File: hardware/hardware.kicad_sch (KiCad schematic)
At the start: 1 part, among them U1 CH32V003F4P6

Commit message: add ch32v003 on pcb
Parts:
- added C1, C10, C11, C12, C13, C14, C15, C16, C17, C18, C19, C2, C20, C21, C22, C23, C24, C25, C26, C27, C28, C29, C30, C31, C32, C33, C34, C35, C36, C37, C38, C39, C40, C41, C42, C43, C44, C45, C46, C47, C48, C49, C50, C51, C52, C53, C54, C7, C8, C9: C_Small, Capacitor_SMD:C_0603_1608Metric, symbol Device:C_Small
- added C3, C4, C5, C6: C, Capacitor_SMD:C_0603_1608Metric, symbol Device:C
- added D1, D10, D11, D12, D13, D14, D15, D16, D17, D18, D19, D2, D20, D21, D22, D23, D24, D3, D4, D5, D6, D7, D8, D9: LED, LED_SMD:LED_0603_1608Metric, symbol Device:LED
- added J1: USB_B_Micro, Connector_USB:USB_Micro-B_Amphenol_10118194_Horizontal, symbol Connector:USB_B_Micro
- added R1, R10, R11, R12, R13, R14, R15, R16, R17, R18, R19, R2, R20, R21, R22, R23, R24, R25, R26, R3, R4, R5, R6, R7, R8, R9: R_Small, Resistor_SMD:R_0603_1608Metric, symbol Device:R_Small
- added U10, U11, U12, U13, U14, U15, U16, U17, U18, U19, U2, U20, U21, U22, U23, U24, U25, U26, U27, U5, U6, U7, U8, U9: CH32V003F4P6, CH32V003F4P6:SOP65P640X121-20N, symbol ch32v003:CH32V003F4P6
- added U3: AMS1117-3.3, Package_TO_SOT_SMD:SOT-223-3_TabPin2, symbol Regulator_Linear:AMS1117-3.3
- added U4: CH340C, Package_SO:SOIC-16_3.9x9.9mm_P1.27mm, symbol Interface_USB:CH340C
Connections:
- net SDA: now reaches U1.11 (PC1/SDA/NSS)
- net SDA: now also R2.2, U10.11 (PC1/SDA/NSS), U11.11 (PC1/SDA/NSS), U12.11 (PC1/SDA/NSS), U13.11 (PC1/SDA/NSS), U14.11 (PC1/SDA/NSS), U15.11 (PC1/SDA/NSS), U16.11 (PC1/SDA/NSS), U17.11 (PC1/SDA/NSS), U18.11 (PC1/SDA/NSS), U19.11 (PC1/SDA/NSS), U2.11 (PC1/SDA/NSS), U20.11 (PC1/SDA/NSS), U21.11 (PC1/SDA/NSS), U22.11 (PC1/SDA/NSS), U23.11 (PC1/SDA/NSS), U24.11 (PC1/SDA/NSS), U25.11 (PC1/SDA/NSS), U26.11 (PC1/SDA/NSS), U27.11 (PC1/SDA/NSS), U5.11 (PC1/SDA/NSS), U6.11 (PC1/SDA/NSS), U7.11 (PC1/SDA/NSS), U8.11 (PC1/SDA/NSS), U9.11 (PC1/SDA/NSS)
- net SCL: now reaches U1.12 (PC2/SCL/URTS/T1BKIN)
- net SCL: now also R1.2, U10.12 (PC2/SCL/URTS/T1BKIN), U11.12 (PC2/SCL/URTS/T1BKIN), U12.12 (PC2/SCL/URTS/T1BKIN), U13.12 (PC2/SCL/URTS/T1BKIN), U14.12 (PC2/SCL/URTS/T1BKIN), U15.12 (PC2/SCL/URTS/T1BKIN), U16.12 (PC2/SCL/URTS/T1BKIN), U17.12 (PC2/SCL/URTS/T1BKIN), U18.12 (PC2/SCL/URTS/T1BKIN), U19.12 (PC2/SCL/URTS/T1BKIN), U2.12 (PC2/SCL/URTS/T1BKIN), U20.12 (PC2/SCL/URTS/T1BKIN), U21.12 (PC2/SCL/URTS/T1BKIN), U22.12 (PC2/SCL/URTS/T1BKIN), U23.12 (PC2/SCL/URTS/T1BKIN), U24.12 (PC2/SCL/URTS/T1BKIN), U25.12 (PC2/SCL/URTS/T1BKIN), U26.12 (PC2/SCL/URTS/T1BKIN), U27.12 (PC2/SCL/URTS/T1BKIN), U5.12 (PC2/SCL/URTS/T1BKIN), U6.12 (PC2/SCL/URTS/T1BKIN), U7.12 (PC2/SCL/URTS/T1BKIN), U8.12 (PC2/SCL/URTS/T1BKIN), U9.12 (PC2/SCL/URTS/T1BKIN)
- net DIO0: now reaches U1.18 (PD1/SWIO/T1CH3N/AETR2)
- net RX-PROG: now reaches U1.2 (PD5/UTX/A5)
- net RX-PROG: now also U4.3 (RXD)
- net TX-PROG: now reaches U1.3 (PD6/URX/A6)
- net TX-PROG: now also U4.2 (TXD)
- net GND: now reaches U1.7 (VSS)
- net GND: now also C1.2, C10.2, C11.2, C12.2, C13.2, C14.2, C15.2, C16.2, C17.2, C18.2, C19.2, C2.2, C20.2, C21.2, C22.2, C23.2, C24.2, C25.2, C26.2, C27.2, C28.2, C29.2, C3.2, C30.2, C31.2, C32.2, C33.2, C34.2, C35.2, C36.2, C37.2, C38.2, C39.2, C4.2, C40.2, C41.2, C42.2, C43.2, C44.2, C45.2, C46.2, C47.2, C48.2, C49.2, C5.2, C50.2, C51.2, C52.2, C53.2, C54.2, C6.2, C7.2, C8.2, C9.2, J1.5 (GND), U10.7 (VSS), U11.7 (VSS), U12.7 (VSS), U13.7 (VSS), U14.7 (VSS), U15.7 (VSS), U16.7 (VSS), U17.7 (VSS), U18.7 (VSS), U19.7 (VSS), U2.7 (VSS), U20.7 (VSS), U21.7 (VSS), U22.7 (VSS), U23.7 (VSS), U24.7 (VSS), U25.7 (VSS), U26.7 (VSS), U27.7 (VSS), U3.1 (GND), U4.1 (GND), U5.7 (VSS), U6.7 (VSS), U7.7 (VSS), U8.7 (VSS), U9.7 (VSS)
- net +3V3: now reaches U1.9 (VDD)
- net +3V3: now also C1.1, C10.1, C11.1, C12.1, C13.1, C14.1, C15.1, C16.1, C17.1, C18.1, C19.1, C2.1, C20.1, C21.1, C22.1, C23.1, C24.1, C25.1, C26.1, C27.1, C28.1, C29.1, C30.1, C31.1, C32.1, C33.1, C34.1, C35.1, C36.1, C37.1, C38.1, C39.1, C4.1, C40.1, C41.1, C42.1, C43.1, C44.1, C45.1, C46.1, C47.1, C48.1, C49.1, C5.1, C50.1, C51.1, C52.1, C53.1, C54.1, C6.1, C7.1, C8.1, C9.1, R1.1, R10.2, R11.2, R12.2, R13.2, R14.2, R15.2, R16.2, R17.2, R18.2, R19.2, R2.1, R20.2, R21.2, R22.2, R23.2, R24.2, R25.2, R26.2, R3.2, R4.2, R5.2, R6.2, R7.2, R8.2, R9.2, U10.9 (VDD), U11.9 (VDD), U12.9 (VDD), U13.9 (VDD), U14.9 (VDD), U15.9 (VDD), U16.9 (VDD), U17.9 (VDD), U18.9 (VDD), U19.9 (VDD), U2.9 (VDD), U20.9 (VDD), U21.9 (VDD), U22.9 (VDD), U23.9 (VDD), U24.9 (VDD), U25.9 (VDD), U26.9 (VDD), U27.9 (VDD), U3.2 (VO), U4.16 (VCC), U4.4 (V3), U5.9 (VDD), U6.9 (VDD), U7.9 (VDD), U8.9 (VDD), U9.9 (VDD)
- new net: D16.2 (A), R18.1
- new net: D7.2 (A), R9.1
- new net: D8.2 (A), R10.1
- new net: D16.1 (K), U19.20 (PD3/A4/T2CH2/AETR/UCTS)
- new net: D23.1 (K), U26.20 (PD3/A4/T2CH2/AETR/UCTS)
- new net: D7.1 (K), U10.20 (PD3/A4/T2CH2/AETR/UCTS)
- new net: D14.1 (K), U17.20 (PD3/A4/T2CH2/AETR/UCTS)
- new net: D14.2 (A), R16.1
- new net: D9.1 (K), U12.20 (PD3/A4/T2CH2/AETR/UCTS)
- new net: D24.1 (K), U27.20 (PD3/A4/T2CH2/AETR/UCTS)
- new net: D15.2 (A), R17.1
- new net: D22.1 (K), U25.20 (PD3/A4/T2CH2/AETR/UCTS)
- new net: D22.2 (A), R24.1
- new net: D15.1 (K), U18.20 (PD3/A4/T2CH2/AETR/UCTS)
- new net: D12.2 (A), R14.1
- new net: D19.2 (A), R21.1
- new net: D12.1 (K), U15.20 (PD3/A4/T2CH2/AETR/UCTS)
- new net: D6.2 (A), R8.1
- new net: D6.1 (K), U9.20 (PD3/A4/T2CH2/AETR/UCTS)
- new net: D24.2 (A), R26.1
- new net: D13.1 (K), U16.20 (PD3/A4/T2CH2/AETR/UCTS)
- new net: D13.2 (A), R15.1
- new net: D18.1 (K), U21.20 (PD3/A4/T2CH2/AETR/UCTS)
- new net: D8.1 (K), U11.20 (PD3/A4/T2CH2/AETR/UCTS)
- new net: D9.2 (A), R11.1
- new net: D10.1 (K), U13.20 (PD3/A4/T2CH2/AETR/UCTS)
- new net: D2.1 (K), U5.20 (PD3/A4/T2CH2/AETR/UCTS)
- new net: D2.2 (A), R4.1
- new net: D20.1 (K), U23.20 (PD3/A4/T2CH2/AETR/UCTS)
- new net: D11.1 (K), U14.20 (PD3/A4/T2CH2/AETR/UCTS)
- new net: D11.2 (A), R13.1
- new net: D1.1 (K), U2.20 (PD3/A4/T2CH2/AETR/UCTS)
- new net: D4.1 (K), U7.20 (PD3/A4/T2CH2/AETR/UCTS)
- new net: D4.2 (A), R6.1
- new net: D3.1 (K), U6.20 (PD3/A4/T2CH2/AETR/UCTS)
- new net: D20.2 (A), R22.1
- new net: D5.1 (K), U8.20 (PD3/A4/T2CH2/AETR/UCTS)
- new net: D5.2 (A), R7.1
- new net: D10.2 (A), R12.1
- new net: D23.2 (A), R25.1
- new net: D17.1 (K), U20.20 (PD3/A4/T2CH2/AETR/UCTS)
- new net: D17.2 (A), R19.1
- new net: D21.2 (A), R23.1
- new net: D18.2 (A), R20.1
- new net: D19.1 (K), U22.20 (PD3/A4/T2CH2/AETR/UCTS)
- new net: D1.2 (A), R3.1
- new net: D3.2 (A), R5.1
- new net: D21.1 (K), U24.20 (PD3/A4/T2CH2/AETR/UCTS)
- new net +5V: C3.1, J1.1 (VBUS), U3.3 (VI)
- new net D+: J1.3 (D+), U4.5 (UD+)
- new net D-: J1.2 (D-), U4.6 (UD-)
- new net DIO1: U10.18 (PD1/SWIO/T1CH3N/AETR2), U11.18 (PD1/SWIO/T1CH3N/AETR2), U12.18 (PD1/SWIO/T1CH3N/AETR2), U13.18 (PD1/SWIO/T1CH3N/AETR2), U14.18 (PD1/SWIO/T1CH3N/AETR2), U15.18 (PD1/SWIO/T1CH3N/AETR2), U16.18 (PD1/SWIO/T1CH3N/AETR2), U17.18 (PD1/SWIO/T1CH3N/AETR2), U18.18 (PD1/SWIO/T1CH3N/AETR2), U19.18 (PD1/SWIO/T1CH3N/AETR2), U2.18 (PD1/SWIO/T1CH3N/AETR2), U20.18 (PD1/SWIO/T1CH3N/AETR2), U21.18 (PD1/SWIO/T1CH3N/AETR2), U22.18 (PD1/SWIO/T1CH3N/AETR2), U23.18 (PD1/SWIO/T1CH3N/AETR2), U24.18 (PD1/SWIO/T1CH3N/AETR2), U25.18 (PD1/SWIO/T1CH3N/AETR2), U26.18 (PD1/SWIO/T1CH3N/AETR2), U27.18 (PD1/SWIO/T1CH3N/AETR2), U5.18 (PD1/SWIO/T1CH3N/AETR2), U6.18 (PD1/SWIO/T1CH3N/AETR2), U7.18 (PD1/SWIO/T1CH3N/AETR2), U8.18 (PD1/SWIO/T1CH3N/AETR2), U9.18 (PD1/SWIO/T1CH3N/AETR2)
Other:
- note added: "CONNECTOR"
- note added: "PROGRAM"
- note added: "REGULATOR"
- moved on the sheet: U1

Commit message: add wiring ch32v006
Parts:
- added D25: LED, LED_SMD:LED_0603_1608Metric, symbol Device:LED
- added J2: RJ45_Hanrun_HR911105A_Horizontal, Connector_RJ:RJ45_Hanrun_HR911105A_Horizontal, symbol Connector:RJ45_Hanrun_HR911105A_Horizontal
- added J3: Conn_02x05_Odd_Even, symbol Connector_Generic:Conn_02x05_Odd_Even
- added R27, R28, R29: R_Small, Resistor_SMD:R_0603_1608Metric, symbol Device:R_Small
- added TP1, TP10, TP11, TP12, TP13, TP14, TP15, TP16, TP17, TP18, TP19, TP2, TP20, TP21, TP22, TP23, TP24, TP25, TP3, TP4, TP5, TP6, TP7, TP8, TP9: TestPoint, TestPoint:TestPoint_Pad_1.0x1.0mm, symbol Connector:TestPoint
- added U28: CH32V307RCT6, symbol WCH:CH32V307RCT6
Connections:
- net +3V3: now also J2.4 (TCT), J2.5 (RCT), J3.7 (Pin_7), R27.2, R28.1, R29.1
- net GND: now also J2.8, J2.SH, J3.5 (Pin_5), U28.12 (VSSA), U28.18 (VSS_4), U28.31 (VSS_1), U28.47 (VSS_2), U28.63 (VSS_3)
- net at U1.20 (PD3/A4/T2CH2/AETR/UCTS): now also D25.1 (K)
- net DIO0: no longer names the net of U1.18 (PD1/SWIO/T1CH3N/AETR2)
- net DIO0: now also TP25.1
- removed net DIO1: U10.18 (PD1/SWIO/T1CH3N/AETR2), U11.18 (PD1/SWIO/T1CH3N/AETR2), U12.18 (PD1/SWIO/T1CH3N/AETR2), U13.18 (PD1/SWIO/T1CH3N/AETR2), U14.18 (PD1/SWIO/T1CH3N/AETR2), U15.18 (PD1/SWIO/T1CH3N/AETR2), U16.18 (PD1/SWIO/T1CH3N/AETR2), U17.18 (PD1/SWIO/T1CH3N/AETR2), U18.18 (PD1/SWIO/T1CH3N/AETR2), U19.18 (PD1/SWIO/T1CH3N/AETR2), U2.18 (PD1/SWIO/T1CH3N/AETR2), U20.18 (PD1/SWIO/T1CH3N/AETR2), U21.18 (PD1/SWIO/T1CH3N/AETR2), U22.18 (PD1/SWIO/T1CH3N/AETR2), U23.18 (PD1/SWIO/T1CH3N/AETR2), U24.18 (PD1/SWIO/T1CH3N/AETR2), U25.18 (PD1/SWIO/T1CH3N/AETR2), U26.18 (PD1/SWIO/T1CH3N/AETR2), U27.18 (PD1/SWIO/T1CH3N/AETR2), U5.18 (PD1/SWIO/T1CH3N/AETR2), U6.18 (PD1/SWIO/T1CH3N/AETR2), U7.18 (PD1/SWIO/T1CH3N/AETR2), U8.18 (PD1/SWIO/T1CH3N/AETR2), U9.18 (PD1/SWIO/T1CH3N/AETR2)
- new net: TP23.1, U26.18 (PD1/SWIO/T1CH3N/AETR2)
- new net: TP8.1, U10.18 (PD1/SWIO/T1CH3N/AETR2)
- new net: TP15.1, U12.18 (PD1/SWIO/T1CH3N/AETR2)
- new net: TP24.1, U27.18 (PD1/SWIO/T1CH3N/AETR2)
- new net: D25.2 (A), R27.1
- new net: TP13.1, U18.18 (PD1/SWIO/T1CH3N/AETR2)
- new net: TP5.1, U8.18 (PD1/SWIO/T1CH3N/AETR2)
- new net: TP18.1, U21.18 (PD1/SWIO/T1CH3N/AETR2)
- new net: TP11.1, U17.18 (PD1/SWIO/T1CH3N/AETR2)
- new net: TP10.1, U15.18 (PD1/SWIO/T1CH3N/AETR2)
- new net: J2.12, R28.2
- new net: J2.9, R29.2
- new net: TP6.1, U9.18 (PD1/SWIO/T1CH3N/AETR2)
- new net: TP9.1, U14.18 (PD1/SWIO/T1CH3N/AETR2)
- new net: TP14.1, U19.18 (PD1/SWIO/T1CH3N/AETR2)
- new net: TP16.1, U13.18 (PD1/SWIO/T1CH3N/AETR2)
- new net: TP3.1, U6.18 (PD1/SWIO/T1CH3N/AETR2)
- new net: TP7.1, U11.18 (PD1/SWIO/T1CH3N/AETR2)
- new net: TP22.1, U25.18 (PD1/SWIO/T1CH3N/AETR2)
- new net: TP1.1, U2.18 (PD1/SWIO/T1CH3N/AETR2)
- new net: TP20.1, U23.18 (PD1/SWIO/T1CH3N/AETR2)
- new net: TP4.1, U7.18 (PD1/SWIO/T1CH3N/AETR2)
- new net: TP2.1, U5.18 (PD1/SWIO/T1CH3N/AETR2)
- new net: TP19.1, U22.18 (PD1/SWIO/T1CH3N/AETR2)
- new net: TP12.1, U16.18 (PD1/SWIO/T1CH3N/AETR2)
- new net: TP21.1, U24.18 (PD1/SWIO/T1CH3N/AETR2)
- new net: TP17.1, U20.18 (PD1/SWIO/T1CH3N/AETR2)
- new net BOOT0: U28.60 (BOOT0)
- new net BOOT1: U28.28 (BOOT1/PB2)
- new net LED1: J2.11, U28.51 (PC10)
- new net LED2: J2.10, U28.52 (PC11)
- new net RDN: J2.6 (RD-), U28.38 (PC7/RXN)
- new net RDP: J2.3 (RD+), U28.37 (PC6/RXP)
- new net RST: J3.10 (Pin_10), U28.7 (NRST)
- new net RX: J3.4 (Pin_4)
- new net SWCLK: J3.1 (Pin_1), U28.49 (SWCLK/PA14)
- new net SWDIO: J3.3 (Pin_3), U28.46 (SWDIO/PA13)
- new net TDN: J2.2 (TD-), U28.40 (PC9/TXN)
- new net TDP: J2.1 (TD+), U28.39 (PC8/TXP)
- new net TX: J3.2 (Pin_2)
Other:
- moved on the sheet: C42, C50, D20, R22, U23

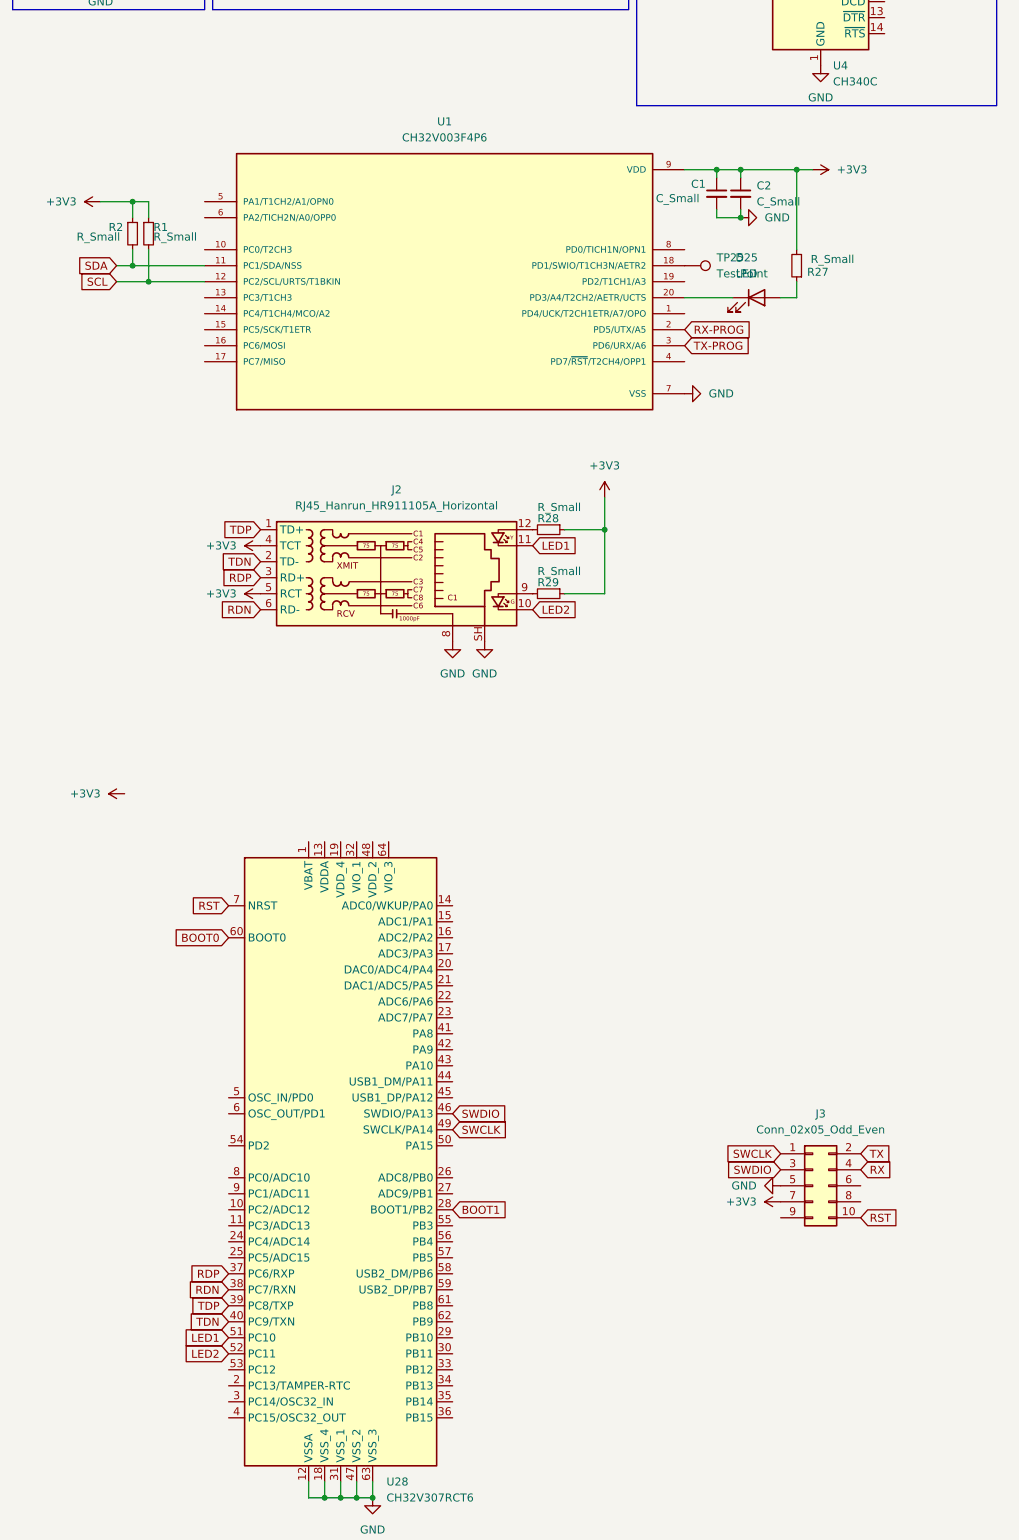
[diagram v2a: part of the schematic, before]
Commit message: add ethernet wiring
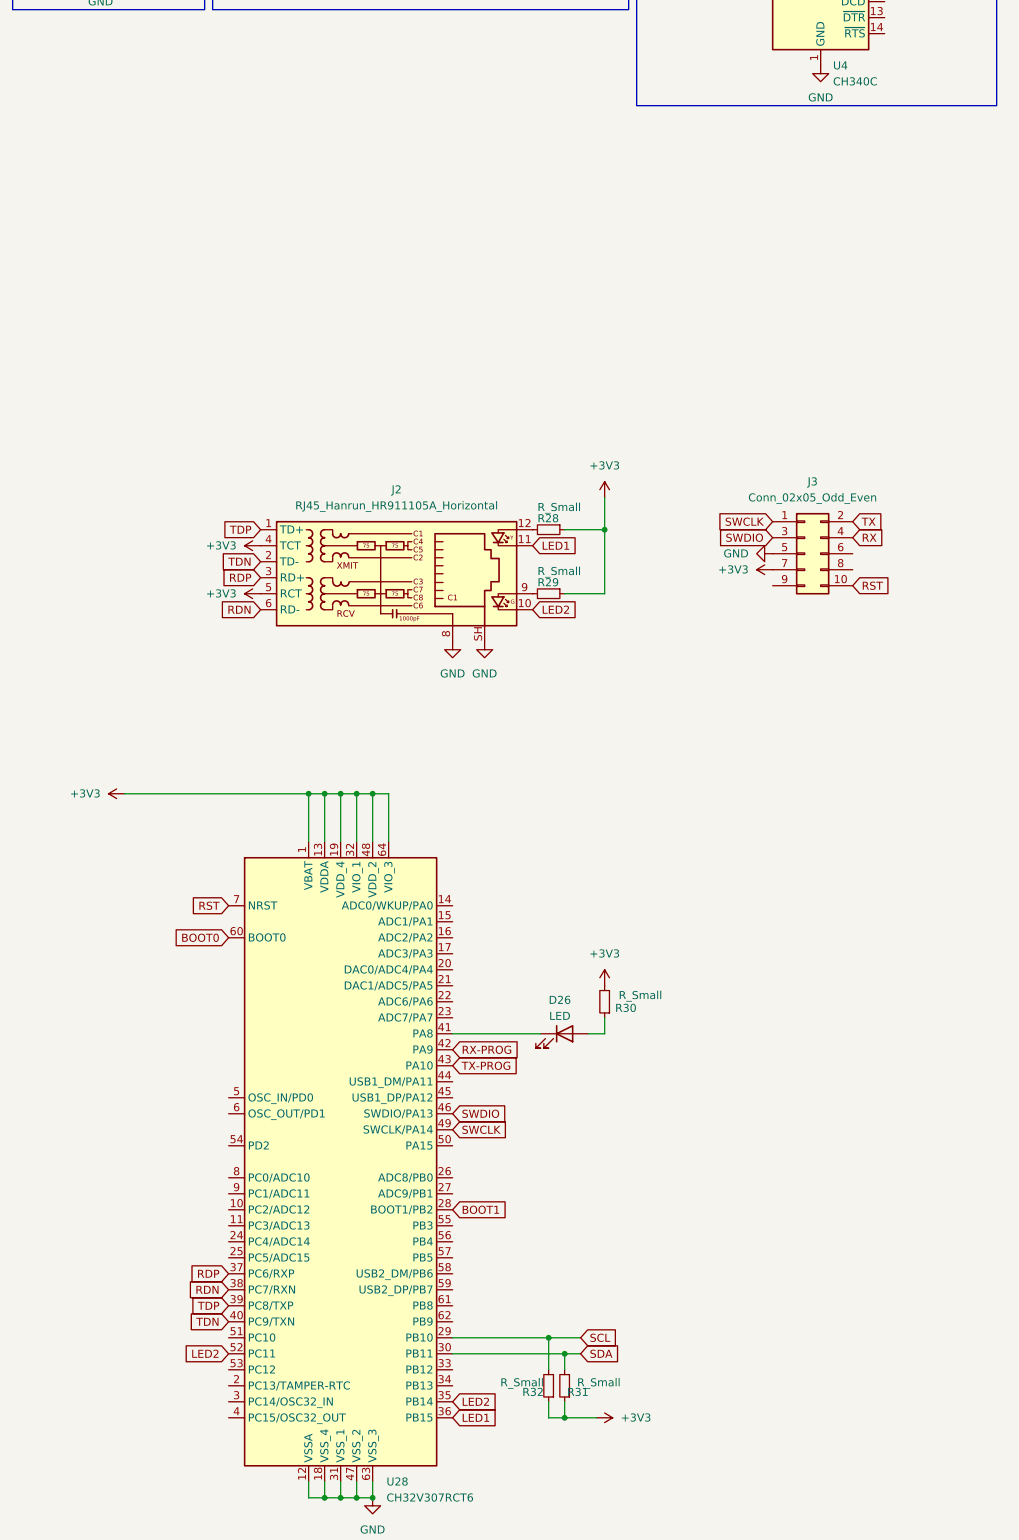
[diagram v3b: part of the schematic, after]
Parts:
- removed C1, C2: C_Small, Capacitor_SMD:C_0603_1608Metric, symbol Device:C_Small
- removed D25: LED, LED_SMD:LED_0603_1608Metric, symbol Device:LED
- removed R1, R2, R27: R_Small, Resistor_SMD:R_0603_1608Metric, symbol Device:R_Small
- removed TP25: TestPoint, TestPoint:TestPoint_Pad_1.0x1.0mm, symbol Connector:TestPoint
- removed U1: CH32V003F4P6, CH32V003F4P6:SOP65P640X121-20N, symbol ch32v003:CH32V003F4P6
- added D26: LED, LED_SMD:LED_0603_1608Metric, symbol Device:LED
- added R30, R31, R32: R_Small, Resistor_SMD:R_0603_1608Metric, symbol Device:R_Small
- J3: footprint (none) -> Connector_PinHeader_2.54mm:PinHeader_2x05_P2.54mm_Vertical
- U28: footprint (none) -> Package_QFP:LQFP-64_10x10mm_P0.5mm
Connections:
- net +3V3: now also U28.1 (VBAT), U28.13 (VDDA), U28.19 (VDD_4), U28.32 (VIO_1), U28.48 (VDD_2), U28.64 (VIO_3), R30.2, R31.1, R32.1
- net LED1: now also U28.36 (PB15); no longer U28.51 (PC10)
- net LED2: now also U28.35 (PB14)
- net RX-PROG: now also U28.42 (PA9)
- net SCL: now also U28.29 (PB10), R32.2
- net SDA: now also U28.30 (PB11), R31.2
- net TX-PROG: now also U28.43 (PA10)
- net at U28.41 (PA8): now also D26.1 (K)
- new net: D26.2 (A), R30.1
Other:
- moved on the sheet: J3

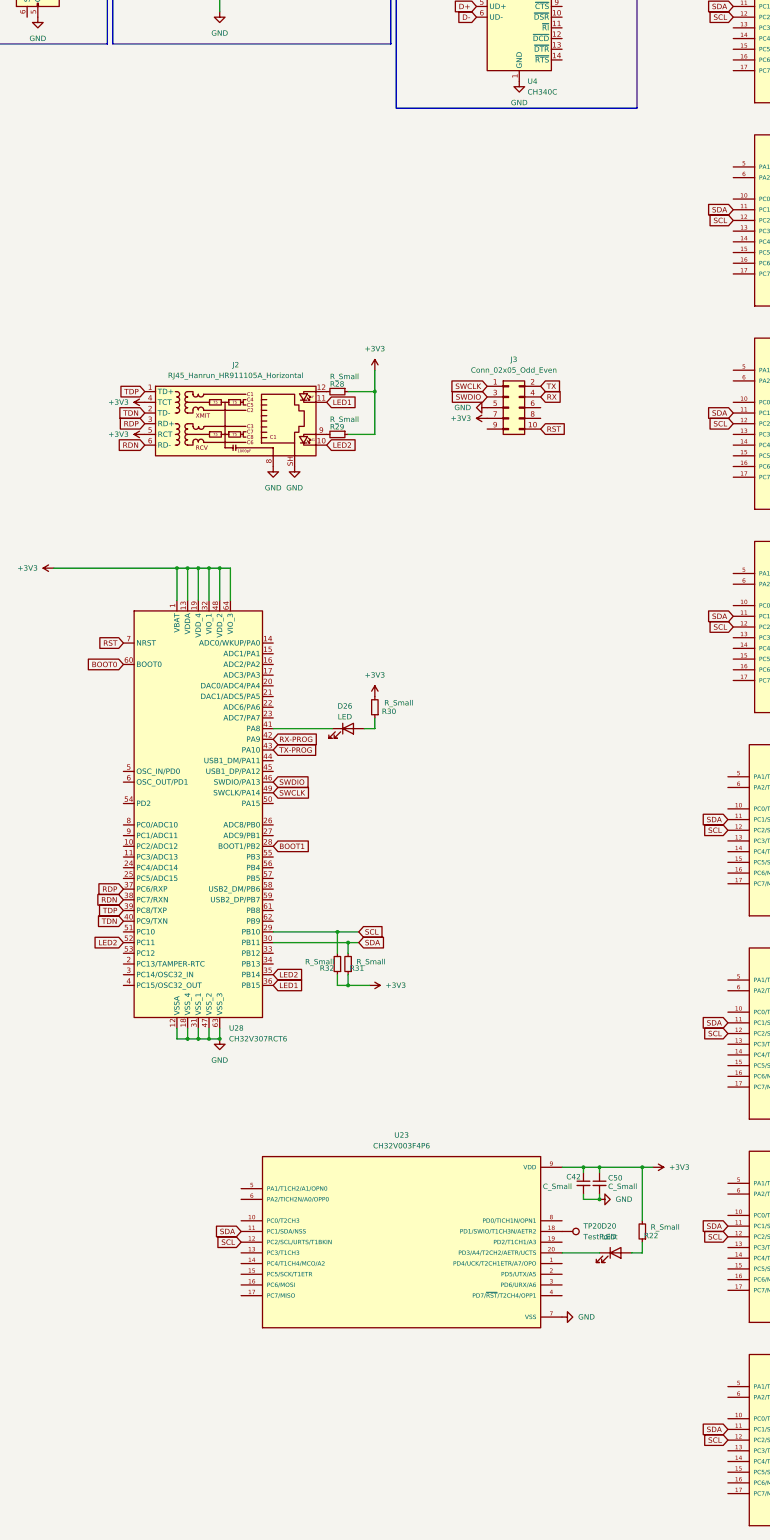
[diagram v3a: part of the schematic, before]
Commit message: wiring ch32v307 + ethernet
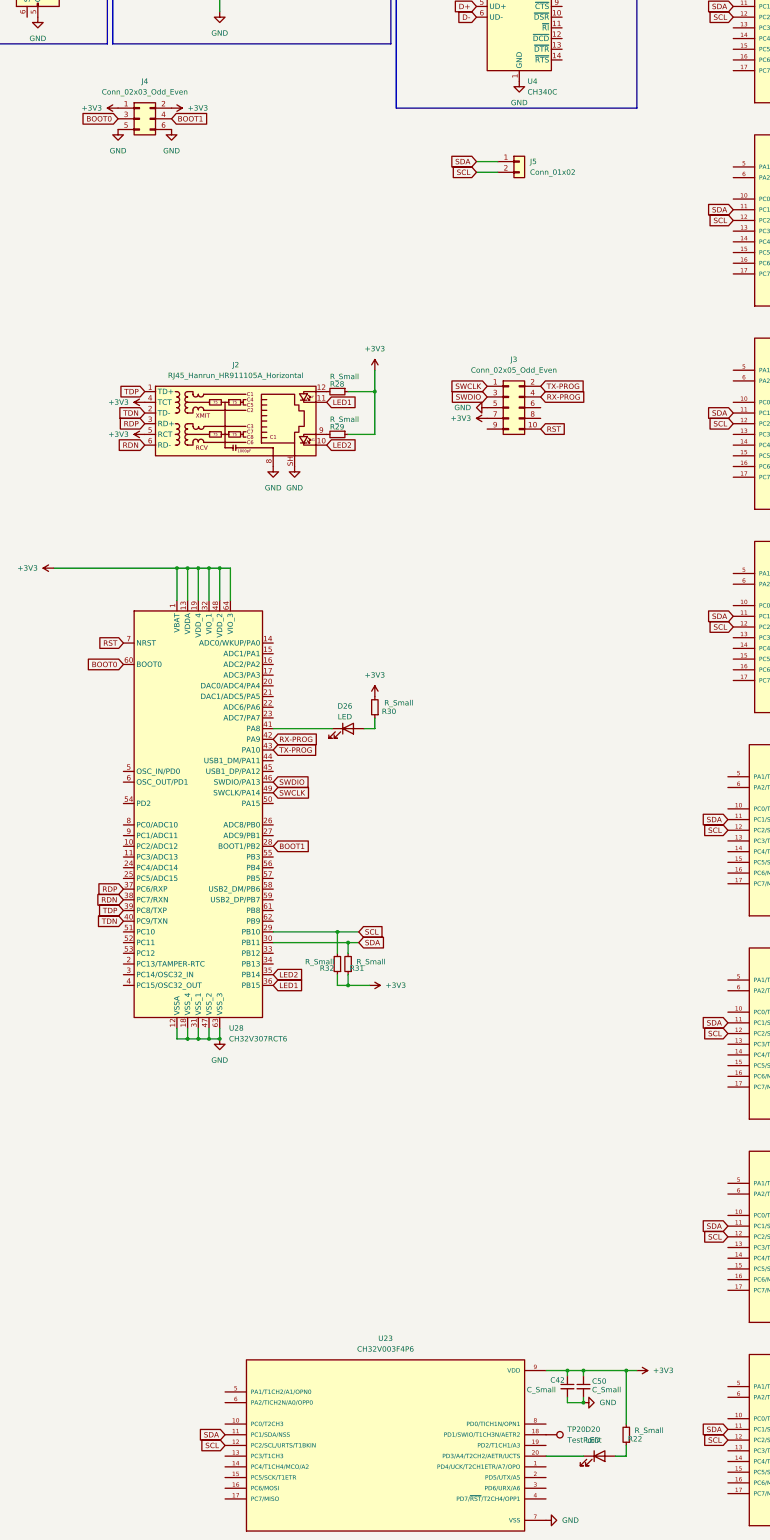
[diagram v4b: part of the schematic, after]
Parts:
- added J4: Conn_02x03_Odd_Even, Connector_PinHeader_2.54mm:PinHeader_2x03_P2.54mm_Vertical, symbol Connector_Generic:Conn_02x03_Odd_Even
- added J5: Conn_01x02, Connector_PinHeader_2.54mm:PinHeader_1x02_P2.54mm_Vertical, symbol Connector_Generic:Conn_01x02
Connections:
- net RX is gone; now on net RX-PROG: J3.4 (Pin_4)
- net TX is gone; now on net TX-PROG: J3.2 (Pin_2)
- net +3V3: now also J4.1 (Pin_1), J4.2 (Pin_2)
- net BOOT0: now also J4.3 (Pin_3)
- net BOOT1: now also J4.4 (Pin_4)
- net GND: now also J4.5 (Pin_5), J4.6 (Pin_6)
- net LED2: no longer U28.52 (PC11)
- net SCL: now also J5.2 (Pin_2)
- net SDA: now also J5.1 (Pin_1)
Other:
- moved on the sheet: C42, C50, D20, R22, TP20, U23
